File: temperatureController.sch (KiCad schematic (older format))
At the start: 39 parts, among them J1 Barrel_Jack, J2 Screw_Terminal_01x02, J3 Conn_01x06, J4 Conn_01x08_Male, J5 Conn_02x02_Odd_Even, Q1 Q_NPN_Darlington_BCE, Q2 Q_NMOS_GSD, U1 MAX7219, U2 MCP6L02x-xSN

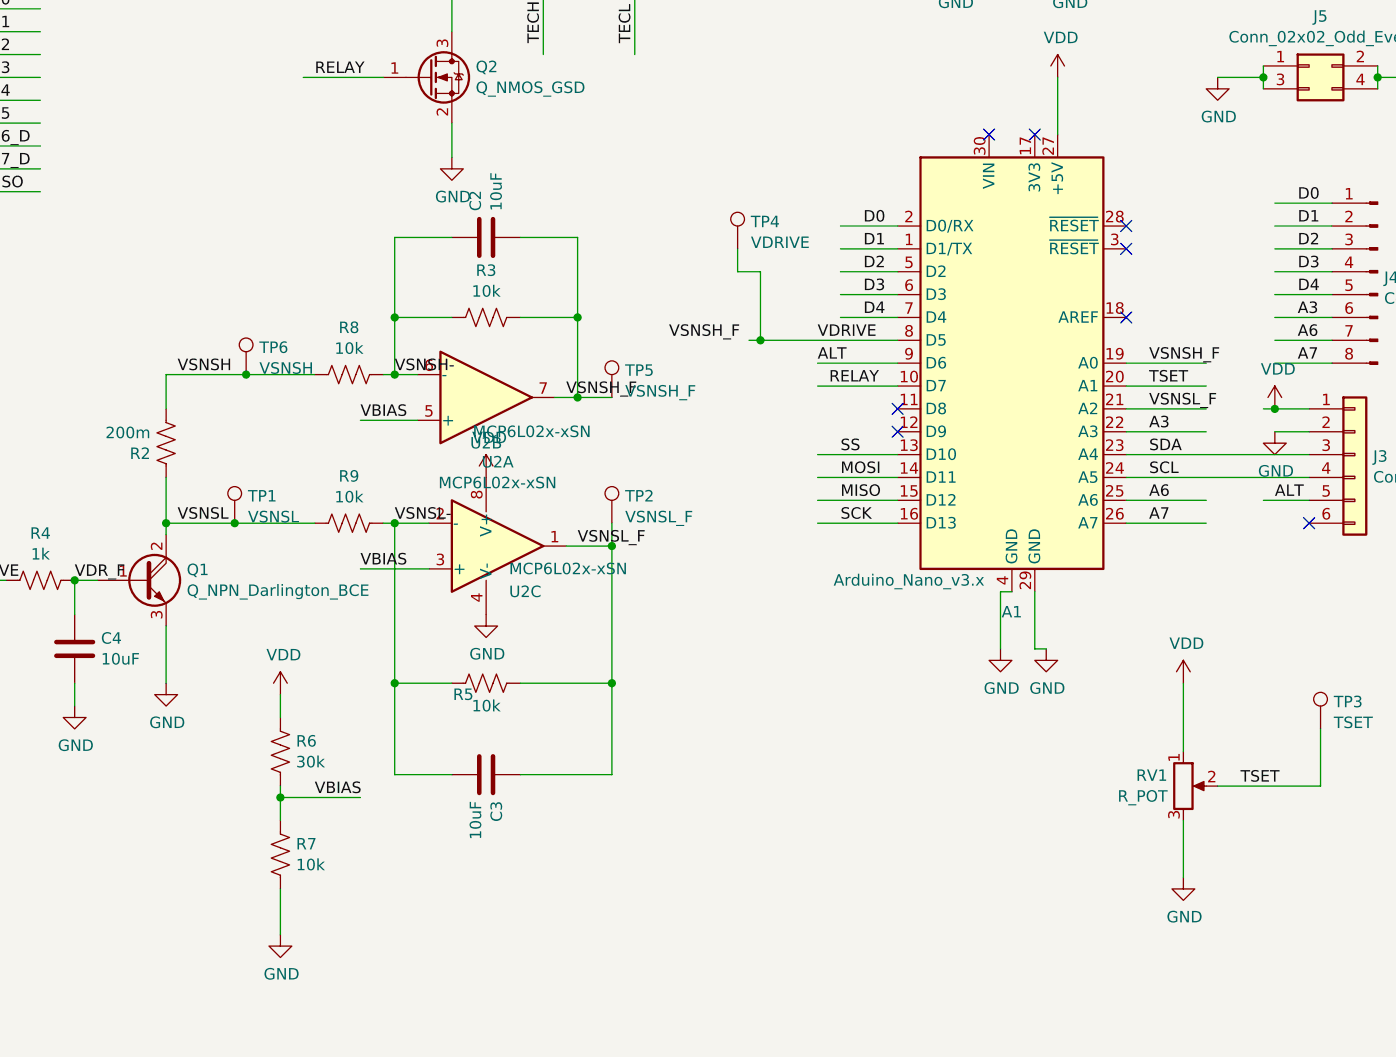
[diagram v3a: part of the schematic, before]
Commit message: updated README, bill of materials with new components and capabilities. Fixed PCB to have a differential amplifier to properly bias the nano's ADC.
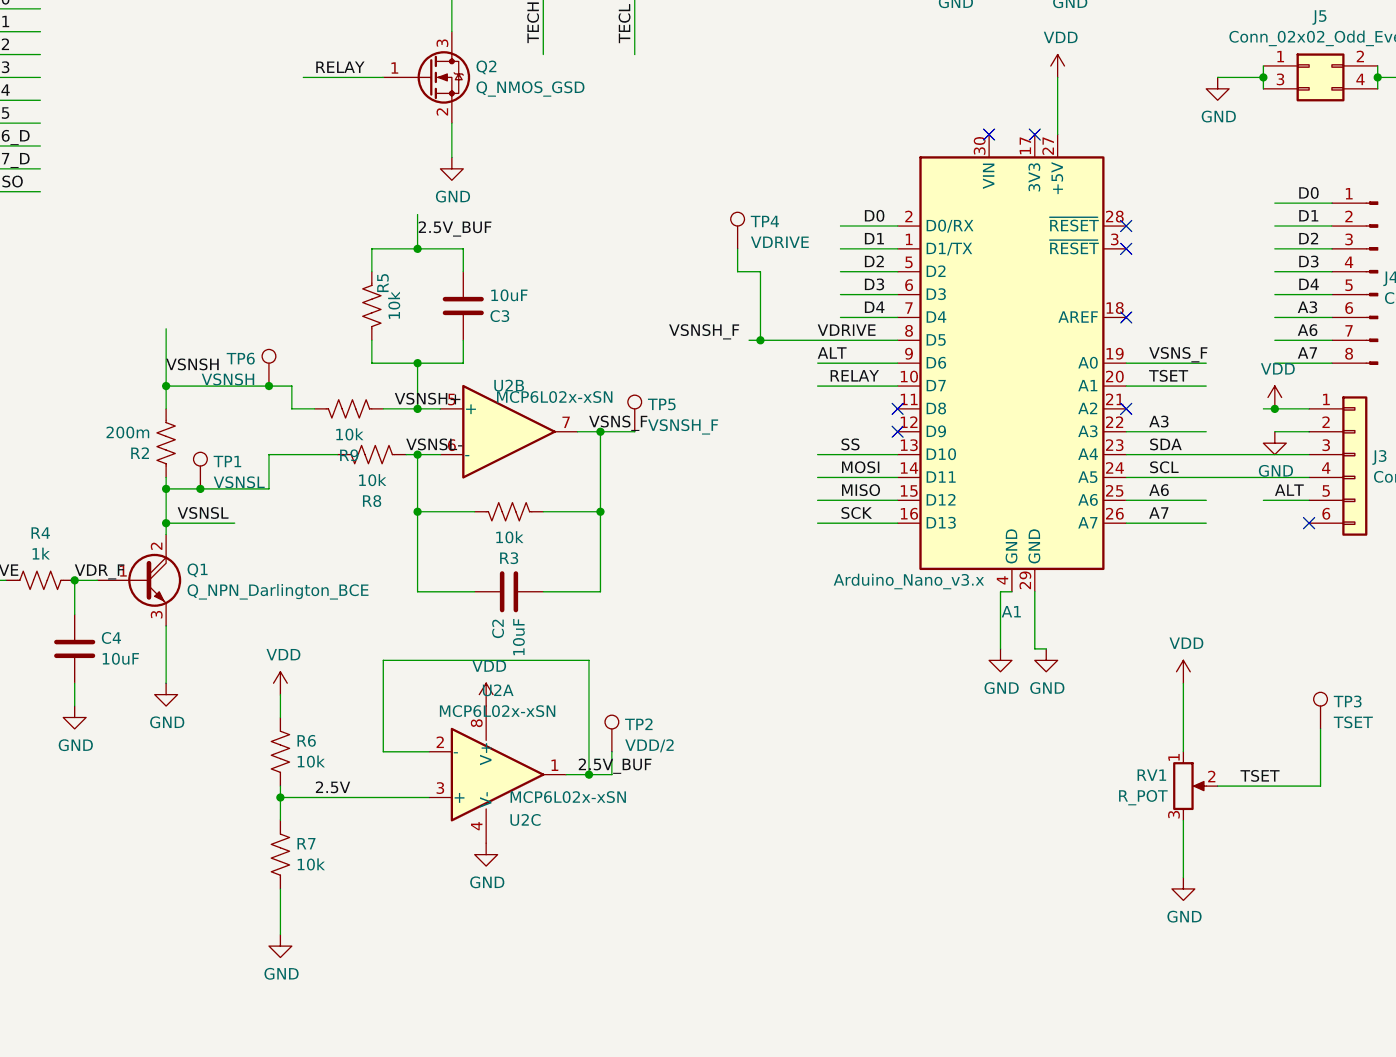
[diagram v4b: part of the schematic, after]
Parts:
- R6: value 30k -> 10k
- TP2: value VSNSL_F -> VDD/2
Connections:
- net labels added: 2.5V, 2.5V_BUF, VSNSH+, VSNS_F
- net labels removed: VBIAS, VSNSH-, VSNSL_F
- wire segments 159 -> 170
- no-connect marks 9 -> 10
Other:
- moved on the sheet: C2, C3, R3, R5, R8, R9, TP1, TP2, TP5, TP6, U2A, U2B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

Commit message: tested version 3, works for bidirectional current control up to 4.6A, corresponding to a dT of 15C when one side is attached to a heatsink and actively cooled.
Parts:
- removed C4: 10uF, Capacitor_SMD:C_0805_2012Metric_Pad1.15x1.40mm_HandSolder, symbol Device:C
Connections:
- net labels removed: VSNSH_F
- wire segments 170 -> 168
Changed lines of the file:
@@
 	0    -1   1    0
 $EndComp
-Text Label 7400 3400 0    50   ~ 0
-VSNSH_F
 $Comp
 L Connector:TestPoint TP6
@@
 VSNSL
 $Comp
-L Device:C C4
-U 1 1 600C8DCC
-P 4800 4750
-F 0 "C4" H 4915 4796 50  0000 L CNN
-F 1 "10uF" H 4915 4705 50  0000 L CNN
-F 2 "Capacitor_SMD:C_0805_2012Metric_Pad1.15x1.40mm_HandSolder" H 4838 4600 50  0001 C CNN
-F 3 "~" H 4800 4750 50  0001 C CNN
-	1    4800 4750
-	1    0    0    -1
-$EndComp
-$Comp
-L power:GND #PWR05
-U 1 1 600CA0C5
-P 4800 5000
-F 0 "#PWR05" H 4800 4750 50  0001 C CNN
-F 1 "GND" H 4805 4827 50  0000 C CNN
-F 2 "" H 4800 5000 50  0001 C CNN
-F 3 "" H 4800 5000 50  0001 C CNN
-	1    4800 5000
-	1    0    0    -1
-$EndComp
-Wire Wire Line
-	4800 5000 4800 4900
-Wire Wire Line
-	4800 4600 4800 4450
-Connection ~ 4800 4450
-$Comp
 L Relay:G2RL-2-DC5 RL1
